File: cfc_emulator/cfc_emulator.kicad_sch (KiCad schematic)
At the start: 23 parts, among them J1 pirt_test_conn, J2 PMOD1A, J3 PMOD1B, U1 DS90CR217MTD_NOPBMTD48_TEX-L

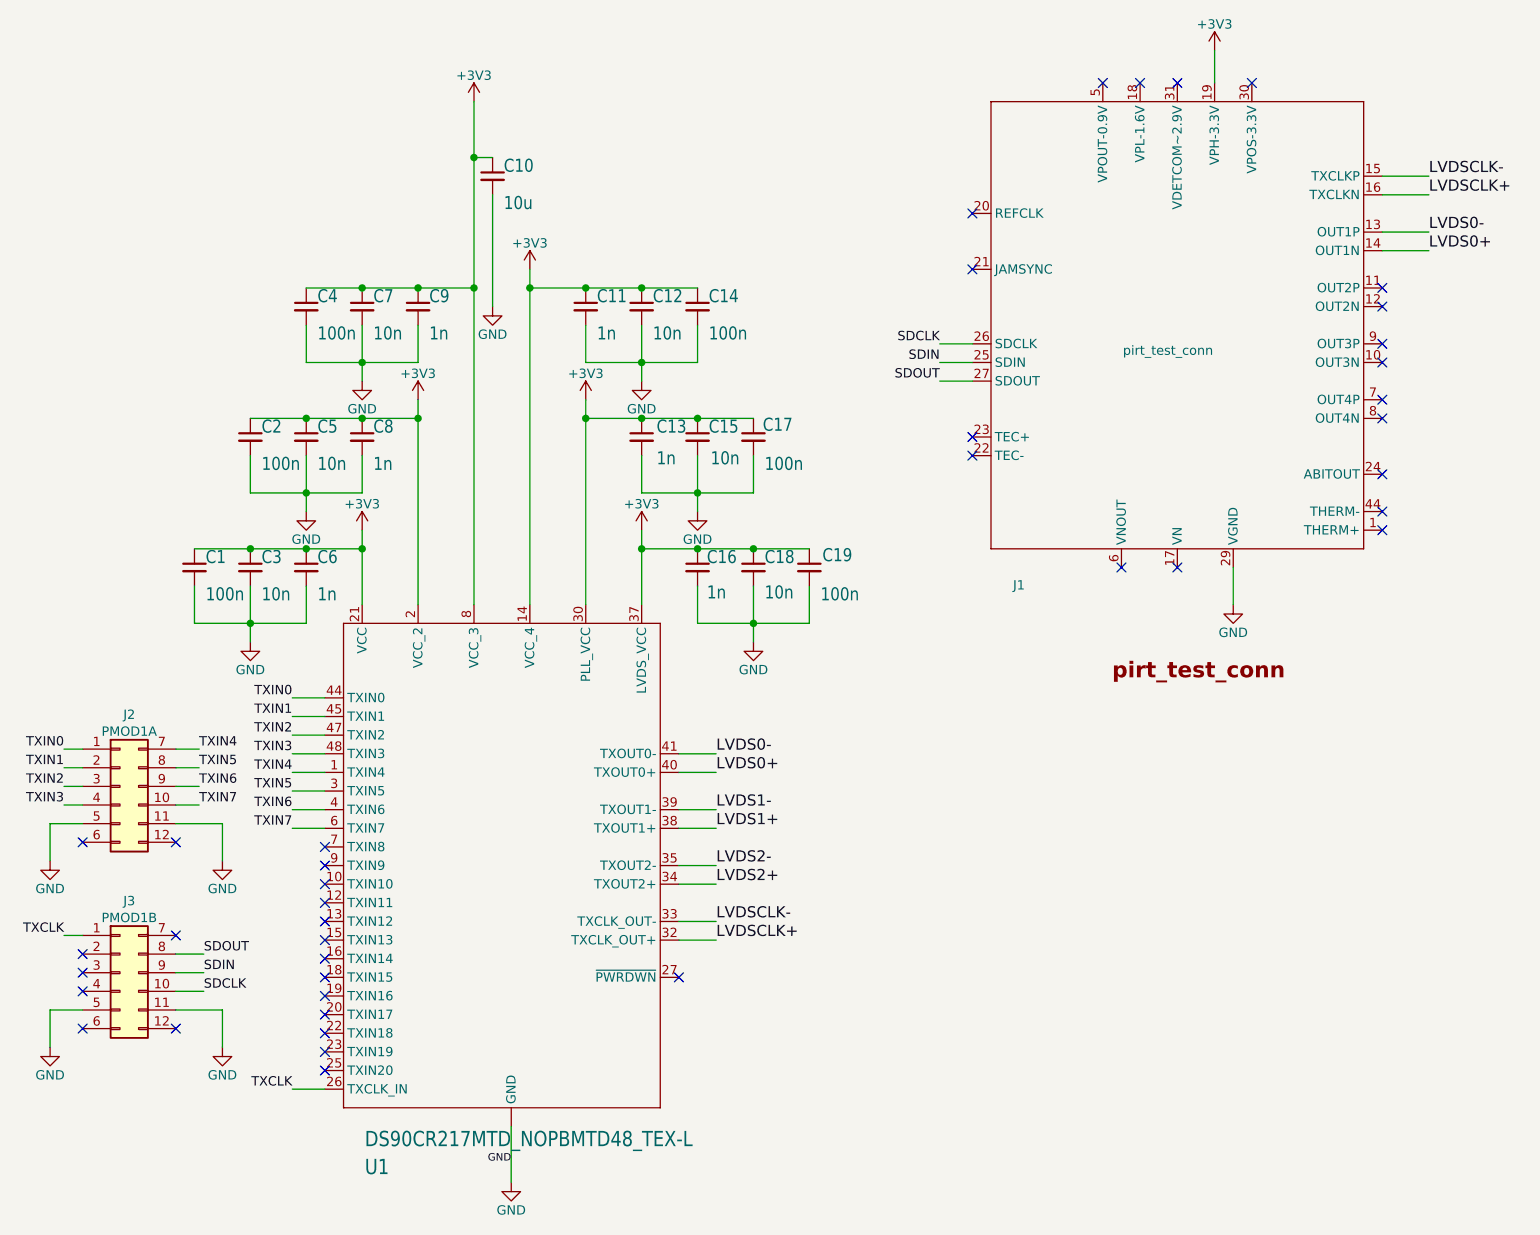
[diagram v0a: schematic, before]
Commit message: Fix ~powerdown handling to add GPIO control from Icebreaker.  Add pullup on ~powerdown to default it to powered up.  Fix footprint error on TX chip (two pins swapped).  Fix pin swap error on both LVDS pairs.  Add test points to ~powerdown and TXCLK
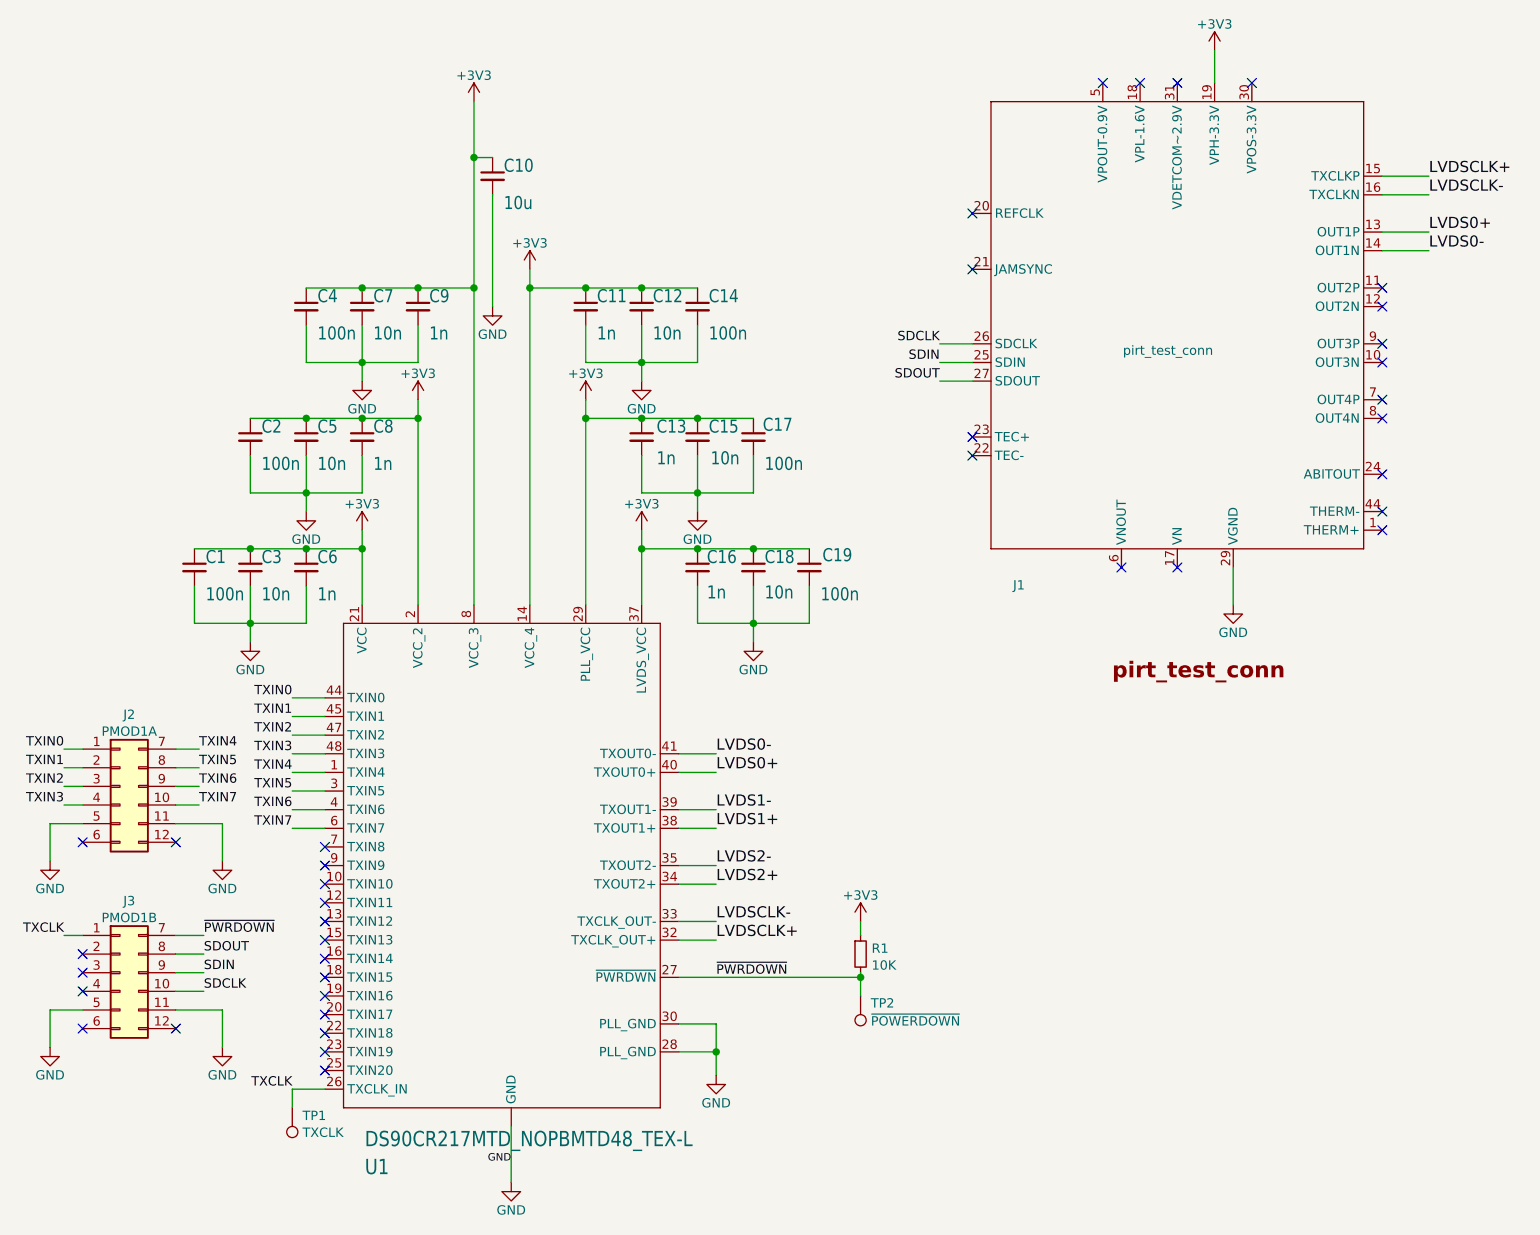
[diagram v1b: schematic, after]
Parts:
- added R1: 10K, Resistor_SMD:R_0603_1608Metric, symbol Device:R_Small
- added TP1: TXCLK, TestPoint:TestPoint_Pad_D2.0mm, symbol Connector:TestPoint
- added TP2: ~POWERDOWN, TestPoint:TestPoint_Pad_D2.0mm, symbol Connector:TestPoint
- C18: footprint Capacitor_SMD:C_0402_1005Metric_Pad0.74x0.62mm_HandSolder -> Capacitor_SMD:C_0603_1608Metric_Pad1.08x0.95mm_HandSolder
- C2: footprint Capacitor_SMD:C_0402_1005Metric_Pad0.74x0.62mm_HandSolder -> Capacitor_SMD:C_0805_2012Metric_Pad1.18x1.45mm_HandSolder
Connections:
- net +3V3: now also U1.29 (PLL_VCC), R1.1; no longer U1.30 (PLL_VCC)
- net GND: now also U1.28 (PLL_GND), U1.30 (PLL_GND)
- net LVDS0+: now also J1.13 (OUT1P); no longer J1.14 (OUT1N)
- net LVDS0-: now also J1.14 (OUT1N); no longer J1.13 (OUT1P)
- net LVDSCLK+: now also J1.15 (TXCLKP); no longer J1.16 (TXCLKN)
- net LVDSCLK-: now also J1.16 (TXCLKN); no longer J1.15 (TXCLKP)
- net TXCLK: now also TP1.1
- net ~PWRDOWN: now reaches J3.7 (Pin_7)
- net ~PWRDOWN: now also U1.27 (~PWRDWN), R1.2, TP2.1
- no-connect marks 41 -> 39
